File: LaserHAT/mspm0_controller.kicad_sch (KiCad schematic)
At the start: 12 parts, among them SW6 BSL, SW7 BL-DT (LCSC C53223909), SW8 BACK, SW9 FIRE, U5 AP2171W, U7 MSPM0G3507SRHBR

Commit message: LaserHAT + LaserDaughter: one verified "LCSC Part #" field per part for the Fabrication Toolkit
The schematics carried Rev 1 fields under four spellings ("LCSC Part #", "LCSC Part#",
"LCSC Parth#", "LCSC Part") with stale codes (every 0402 resistor = 47k, TLV2371 = AP2171,
74LVC2G17 = SI3134, zeners = SS14, DMMT5401 = MT3608 ...), which is what the toolkit's BOM showed.

- tools/lcsc_parts.py: every code re-verified against LCSC/JLC (MPN, package, value); LEDs to JLC
  basic KT-0603 (D5 white C2290, D7/D9 red C2286; was extended C5336487), R13 3k -> 2k basic,
  U1 CAT24C32 (out of stock) -> M24C32-WDW6TP C283445 (TSSOP-8, pin-compatible), U5 AP2171
  -> the WG-7 SOT-25 variant C110466 (32k in stock vs 250); VALUES table for the changed parts
- tools/stamp_lcsc.py: writes the table into one "LCSC Part #" field per symbol (text patch of
  the KiCad 9 sheets) and footprint (pcbnew), removes the misspelt variants, sets the Values;
  make_laser_daughter.py stamps its output so the laser sheet stays correct on regeneration
- jlc_fab.py warns when a board field disagrees with the table
- both schematics + boards stamped; ERC/DRC unchanged, path_check 0 mismatches; fab outputs
  regenerated; HAT board backup in stash/LaserDriver_user_2026-09-30_pre-lcsc.kicad_pcb

Co-Authored-By: Claude Fable 5.1 <noreply@anthropic.com>
Claude-Session: https://claude.ai/code/session_018vgLizGzYPynnY93ajvoVA
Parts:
- C2: LCSC Part # C95841 -> C15850
- SW7: LCSC Part # (none) -> C53223909
- SW9: LCSC Part # (none) -> C720477
- U5: LCSC Part # C2680322 -> C110466
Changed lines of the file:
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@@
+			)
+		)
+		(property "LCSC Part #" "C720477"
+			(at 96.52 218.44 0)
+			(effects
+				(font
+					(size 1.27 1.27)
+				)
+				(hide yes)
 			)
 		)
@@
 			)
 		)
-		(property "LCSC Part #" "C95841"
+		(property "LCSC Part #" "C15850"
 			(at 85.09 121.92 0)
 			(effects
@@
 			)
 		)
-		(property "LCSC Part #" "C2680322"
+		(property "LCSC Part #" "C110466"
 			(at 95.25 82.55 0)
 			(effects
@@
 			)
 		)
+		(property "LCSC Part #" "C53223909"
+			(at 99.06 190.5 0)
+			(effects
+				(font
+					(size 1.27 1.27)
+				)
+				(hide yes)
+			)
+		)

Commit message: BOM clean-up: one line per part, non-parts excluded, SW10 shield pads unnumbered
- Values unified where the same LCSC part had two spellings (HAT R3 "47k 1%" -> "47k";
  laser R1-R5 drop the " 1%"), so the Fabrication Toolkit merges them into one BOM line
- lcsc_parts.NON_PARTS (solder jumpers, mounting holes, logo, laser J4/TP1): symbol
  "exclude from BOM" + footprint exclude-from-BOM/-position-files, so they no longer show up
  as BOM lines without a part number
- SW10 (MSK12C02) footprint: the four "SH" shield pads are unnumbered now (library + board),
  which removes the F8 warning "no pin SH in symbol"
- verified by running the Fabrication Toolkit's ProcessManager headlessly on both boards:
  HAT 36 BOM lines / 42 CPL rows, laser 24 / 23; ERC, DRC and path_check unchanged

Co-Authored-By: Claude Fable 5.1 <noreply@anthropic.com>
Claude-Session: https://claude.ai/code/session_018vgLizGzYPynnY93ajvoVA
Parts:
- R3: value 47k 1% -> 47k
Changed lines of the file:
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@@
 			)
 		)
-		(property "Value" "47k 1%"
+		(property "Value" "47k"
 			(at 120.65 121.9199 0)
 			(effects

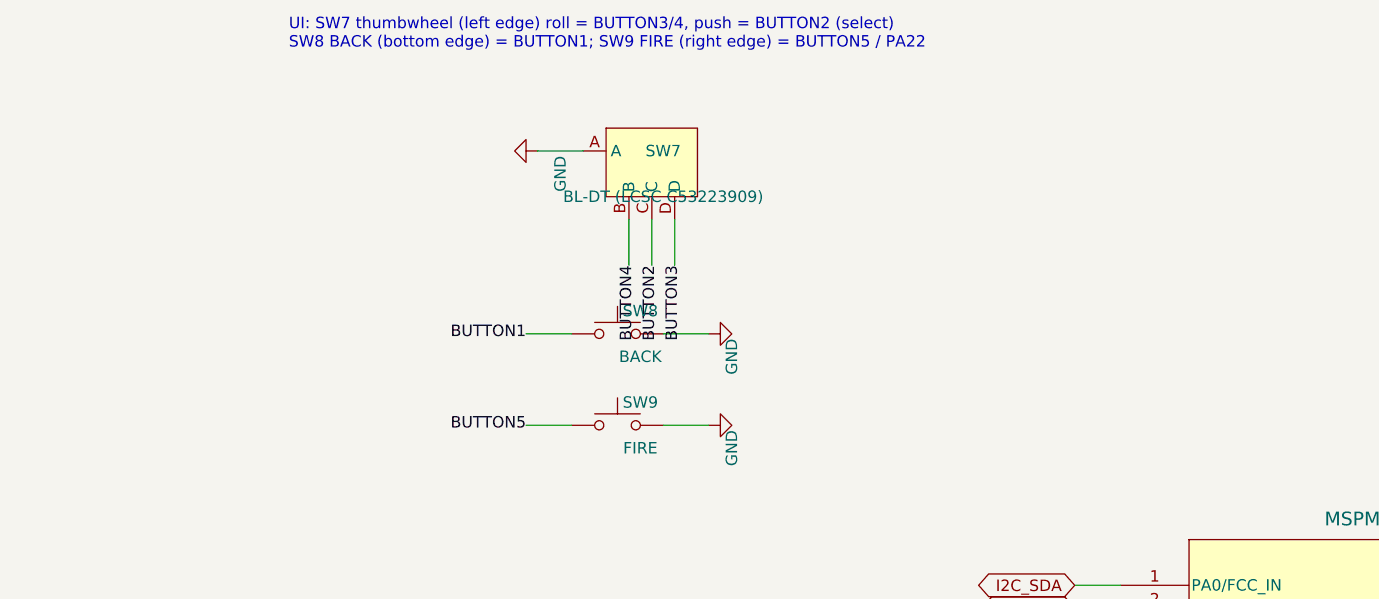
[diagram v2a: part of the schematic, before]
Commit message: BOM: descriptions from the LCSC catalog, value verifier and netlist-vs-board check on all three boards
R15 (2k, C4109) still said "200Ω" in its Description: the Rev 1 symbols carried descriptions and
datasheet links of parts long replaced (R13 "1kΩ", D5 "Emerald Green", D7 "Ice Blue", L1 "22uH 6x6",
Rs1 "10Ω", D3 "1N4148", ...). Now:
- tools/lcsc_catalog.json: LCSC MPN, brand, package, description, parameter table (Resistance /
  Capacitance / Inductance ...) and datasheet URL for every code, fetched by tools/lcsc_verify.py
- stamp_lcsc.py writes Description "<MPN> (<brand>, <package>): <LCSC description>" and the LCSC
  datasheet URL into every machine-placed symbol and footprint (HAT + laser)
- tools/lcsc_verify.py: every R/C/L Value must equal LCSC's parameter, other parts' MPN must match
  the Value (label values like "FIRE" are listed, not failed), size codes must match the package;
  covers HAT, laser and the e-stim list (bom_EStimDaughter.csv) and the fields the toolkit reads:
  0 mismatches on all three boards
- tools/sync_check.py: read-only F8 (parts, footprint ids, values, DNP, pad nets, paths vs the
  exported netlist): 0 differences on all three boards after fixing the owl's missing
  "Footprints:" library prefix and the e-stim U5/U8 paths (netlist uses the other unit's uuid;
  backup in stash/EStimDaughter_2026-09-30_pre-unitpath.kicad_pcb)
- values: laser D1/D3 "SS14" -> "DSK14" (the part ordered), HAT J5 -> "GT-USB-7010ASV"
- fab outputs regenerated; ERC/DRC unchanged

Co-Authored-By: Claude Fable 5.1 <noreply@anthropic.com>
Claude-Session: https://claude.ai/code/session_018vgLizGzYPynnY93ajvoVA
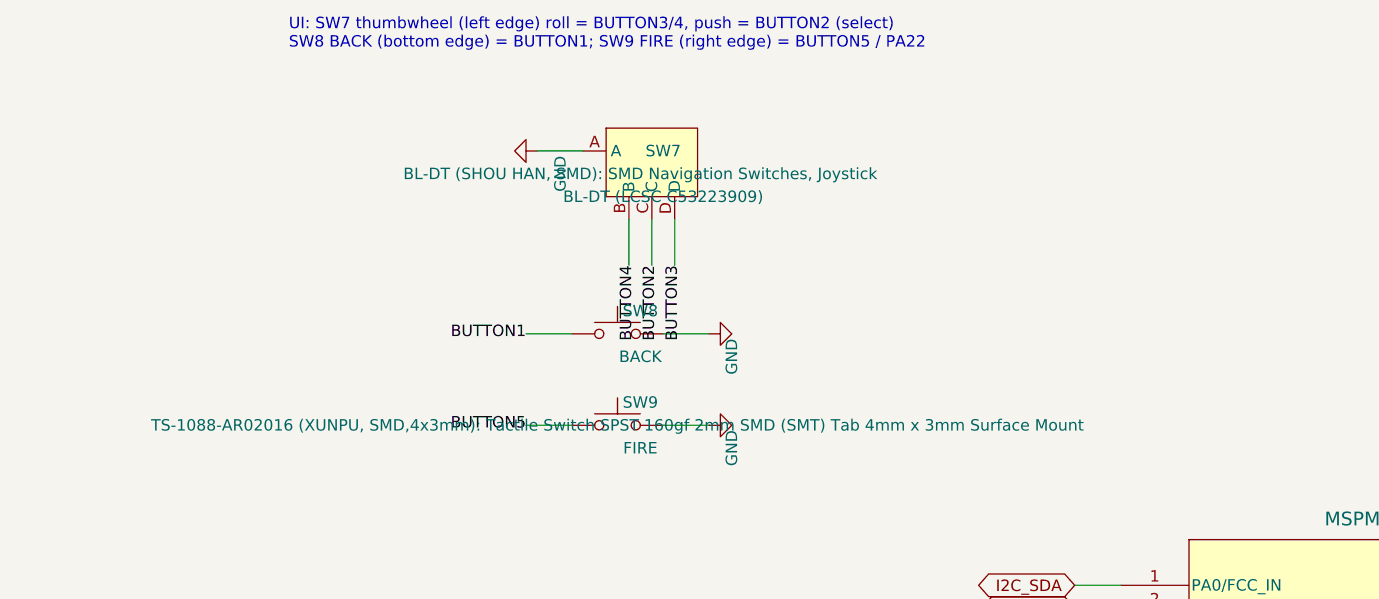
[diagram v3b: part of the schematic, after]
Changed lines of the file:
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@@
 			)
 		)
-		(property "Datasheet" "~"
+		(property "Datasheet" "https://datasheet.lcsc.com/datasheet/pdf/02336ea48ea44ca18c72517dd3cb7b47.pdf?productCode=C307331"
 			(at 74.93 121.92 0)
 			(effects
@@
 			)
 		)
-		(property "Description" "100nF ±10% 50V Ceramic Capacitor X7R 0402"
+		(property "Description" "CL05B104KB54PNC (Samsung Electro-Mechanics, 0402): 100nF ±10% 50V Ceramic Capacitor X7R 0402"
 			(at 74.93 121.92 0)
 			(effects
@@
 			)
 		)
-		(property "Datasheet" ""
+		(property "Datasheet" "https://datasheet.lcsc.com/datasheet/pdf/0475ac02febf455ca9ddcfb380b0df0d.pdf?productCode=C720477"
 			(at 96.52 218.44 0)
 			(effects
@@
 			)
 		)
-		(property "Description" ""
+		(property "Description" "TS-1088-AR02016 (XUNPU, SMD,4x3mm): Tactile Switch SPST 160gf 2mm SMD (SMT) Tab 4mm x 3mm Surface Mount"
 			(at 96.52 218.44 0)
 			(effects
@@
 			)
 		)
-		(property "Datasheet" "~"
+		(property "Datasheet" "https://datasheet.lcsc.com/datasheet/pdf/02336ea48ea44ca18c72517dd3cb7b47.pdf?productCode=C15850"
 			(at 85.09 121.92 0)
 			(effects
@@
 			)
 		)
-		(property "Description" "10uF ±10% 16V Ceramic Capacitor X7R 0805"
+		(property "Description" "CL21A106KAYNNNE (Samsung Electro-Mechanics, 0805): 10uF ±10% 25V Ceramic Capacitor X5R 0805"
 			(at 85.09 121.92 0)
 			(effects
@@
 			)
 		)
-		(property "Description" ""
+		(property "Description" "MSPM0G3507SRHBR (TI, VQFN-32(5x5)): ARM Cortex-M0+ 32 Bit VQFN-32(5x5) Microcontrollers RoHS"
 			(at 152.4 236.22 0)
 			(effects
@@
 			)
 		)
-		(property "Datasheet" "~"
+		(property "Datasheet" "https://datasheet.lcsc.com/datasheet/pdf/02336ea48ea44ca18c72517dd3cb7b47.pdf?productCode=C15195"
 			(at 118.11 134.62 0)
 			(effects
@@
 			)
 		)
-		(property "Description" "10nF ±10% 50V Ceramic Capacitor X7R 0402"
+		(property "Description" "CL05B103KB5NNNC (Samsung Electro-Mechanics, 0402): 10nF ±10% 50V Ceramic Capacitor X7R 0402"
 			(at 118.11 134.62 0)
 			(effects
@@
 			)
 		)
-		(property "Datasheet" "~"
+		(property "Datasheet" "https://datasheet.lcsc.com/datasheet/pdf/b19aead5bee956848397b2fed1f2b97a.pdf?productCode=C844674"
 			(at 139.7 123.19 0)
 			(effects
@@
 			)
 		)
-		(property "Description" "100mW 100kΩ Thin Film Resistor ±25ppm/℃ ±0.1% 0402 Chip Resistor - Surface Mount RoHS"
+		(property "Description" "TNPW0402100KBEED (VISHAY, 0402): 100mW 100kΩ Thin Film Resistor ±25ppm/℃ ±0.1% 0402 Chip Resistor - Surface Mount RoHS"
 			(at 139.7 123.19 0)
 			(effects
@@
 			)
 		)
-		(property "Datasheet" "https://www.diodes.com/assets/Datasheets/AP2161.pdf"
+		(property "Datasheet" "https://datasheet.lcsc.com/datasheet/pdf/dfb41fb13385a5153365608bd440bf80.pdf?productCode=C110466"
 			(at 95.25 81.28 0)
 			(effects
@@
 			)
 		)
-		(property "Description" "Current limited power switch, single channel, SOT-23-5"
+		(property "Description" "AP2171WG-7 (DIODES, SOT-25-5): 1 Active High 1A High Side Switch SOT-25-5 Power Distribution Switches, Load Drivers RoHS"
 			(at 95.25 82.55 0)
 			(effects
@@
 			)
 		)
-		(property "Datasheet" ""
+		(property "Datasheet" "https://datasheet.lcsc.com/datasheet/pdf/22b9f14a2a4b1bb65d3169eedf81cd19.pdf?productCode=C53223909"
 			(at 99.06 190.5 0)
 			(effects
@@
 			)
 		)
-		(property "Description" ""
+		(property "Description" "BL-DT (SHOU HAN, SMD): SMD Navigation Switches, Joystick"
 			(at 99.06 190.5 0)
 			(effects
@@
 			)
 		)
-		(property "Datasheet" "~"
+		(property "Datasheet" "https://datasheet.lcsc.com/datasheet/pdf/0a975aaa49b7c97f38a963127be4a823.pdf?productCode=C25792"
 			(at 118.11 120.65 0)
 			(effects
@@
 			)
 		)
-		(property "Description" "47kΩ ±1% 100mW 0402 Thick Film Resistor AEC-Q200"
+		(property "Description" "0402WGF4702TCE (UNI-ROYAL, 0402): 47kΩ ±1% 62.5mW 0402 Thick Film Resistor"
 			(at 118.11 120.65 0)
 			(effects
@@
 			)
 		)
-		(property "Datasheet" "~"
+		(property "Datasheet" "https://datasheet.lcsc.com/datasheet/pdf/0475ac02febf455ca9ddcfb380b0df0d.pdf?productCode=C720477"
 			(at 368.3 92.71 0)
 			(effects
@@
 			)
 		)
-		(property "Description" "Push button switch, generic, two pins"
+		(property "Description" "TS-1088-AR02016 (XUNPU, SMD,4x3mm): Tactile Switch SPST 160gf 2mm SMD (SMT) Tab 4mm x 3mm Surface Mount"
 			(at 368.3 97.79 0)
 			(effects
@@
 			)
 		)
-		(property "Datasheet" "~"
+		(property "Datasheet" "https://datasheet.lcsc.com/datasheet/pdf/02336ea48ea44ca18c72517dd3cb7b47.pdf?productCode=C47339"
 			(at 163.83 121.92 0)
 			(effects
@@
 			)
 		)
-		(property "Description" "470nF ±10% 16V Ceramic Capacitor X7R 0402"
+		(property "Description" "CL05A474KP5NNNC (Samsung Electro-Mechanics, 0402): 470nF ±10% 10V Ceramic Capacitor X5R 0402"
 			(at 163.83 121.92 0)
 			(effects

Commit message: Fab: nothing JLC does not place may be in its BOM (hand-fitted and DNP parts excluded from BOM too)
JLC's upload rejects "R2,SW8,J1,J6,J7,J8,R1,J9 designators don't exist in the CPL file": a BOM
line without a placement is an error, not a "do not place". So HAND_FIT parts now carry symbol
"exclude from BOM" + footprint exclude-from-BOM and -position-files, NOT_FITTED parts DNP +
exclude-from-BOM (independent of the toolkit's "Exclude DNP" checkbox), e-stim PS1 likewise on
its board. jlc_fab.py classifies from lcsc_parts.HAND_FIT and warns on any flag drift.
Verified with the toolkit's own ProcessManager in both checkbox states: every BOM designator is
in the CPL on all three boards (HAT 30 lines / 42, laser 20 / 23, e-stim 23 / 42).

Co-Authored-By: Claude Fable 5.1 <noreply@anthropic.com>
Claude-Session: https://claude.ai/code/session_018vgLizGzYPynnY93ajvoVA
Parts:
- SW8: now left out of the parts list
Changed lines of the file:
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@@
 		(unit 1)
 		(exclude_from_sim no)
-		(in_bom yes)
+		(in_bom no)
 		(on_board yes)
 		(dnp no)

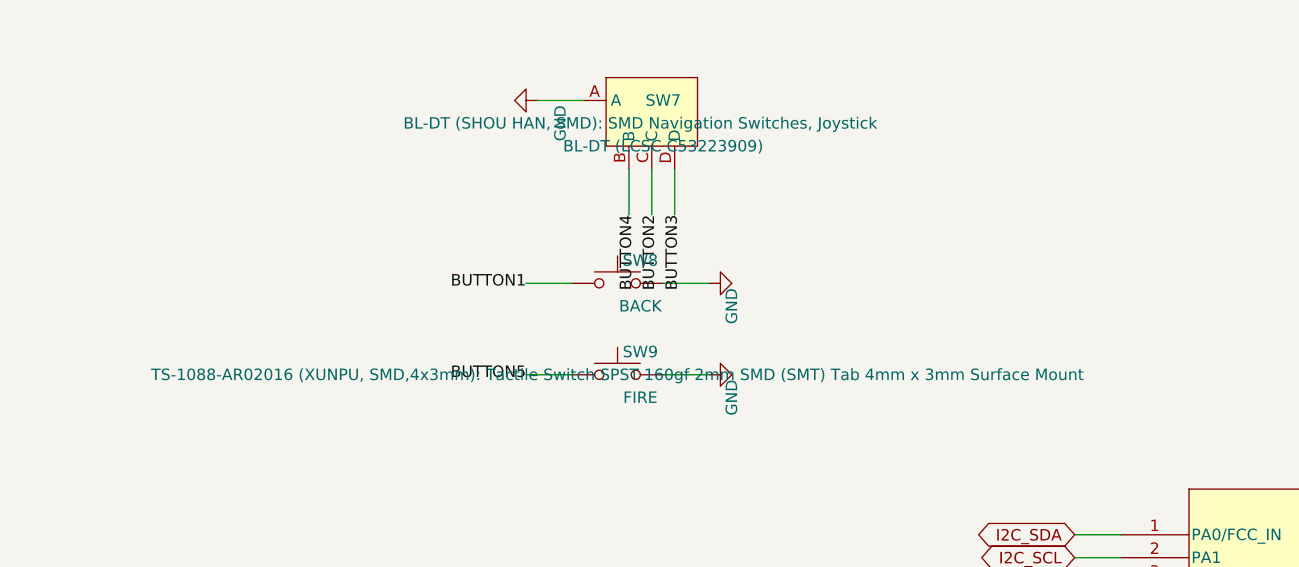
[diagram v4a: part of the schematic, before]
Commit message: LaserHAT: SW8 (BACK) placed by JLC — C&K PTS645VK39-2LFS, C285519
SW8 had been treated as hand-fitted only because it had no LCSC number; JLC assembles
through-hole parts and the PC-pin variant that matches the PTS645Vx39-2LFS footprint is in stock
(6.5k, extended). Stamped into the symbol/footprint, excluded-from flags cleared, verified
against LCSC and the toolkit's BOM/CPL (43 placements now); fab outputs regenerated.

Co-Authored-By: Claude Fable 5.1 <noreply@anthropic.com>
Claude-Session: https://claude.ai/code/session_018vgLizGzYPynnY93ajvoVA
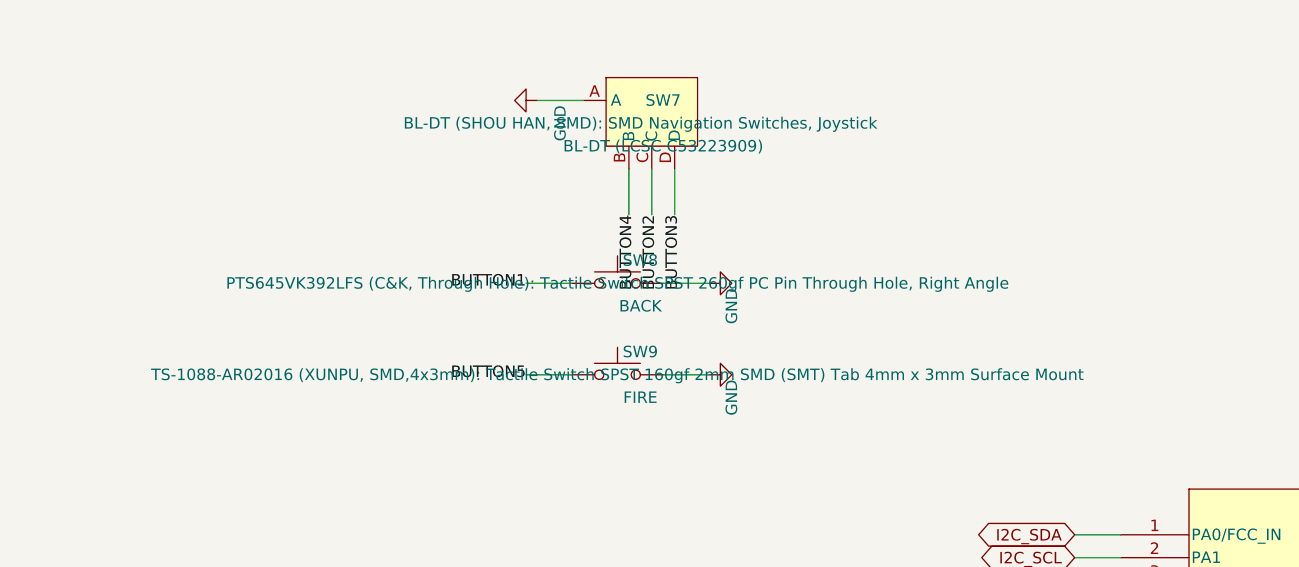
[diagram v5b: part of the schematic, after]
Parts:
- SW8: LCSC Part # (none) -> C285519
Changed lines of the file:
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@@
 			)
 		)
-		(property "Datasheet" ""
+		(property "Datasheet" "https://datasheet.lcsc.com/datasheet/pdf/562a3ff7cc4a11dfb85e5324391a4dcf.pdf?productCode=C285519"
 			(at 96.52 208.28 0)
 			(effects
@@
 			)
 		)
-		(property "Description" ""
+		(property "Description" "PTS645VK392LFS (C&K, Through Hole): Tactile Switch SPST 260gf PC Pin Through Hole, Right Angle"
 			(at 96.52 208.28 0)
 			(effects
@@
 			)
 		)
+		(property "LCSC Part #" "C285519"
+			(at 96.52 208.28 0)
+			(effects
+				(font
+					(size 1.27 1.27)
+				)
+				(hide yes)
+			)
+		)
